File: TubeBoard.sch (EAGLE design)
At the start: 12 parts, among them IC1 HV5530PQFP-44

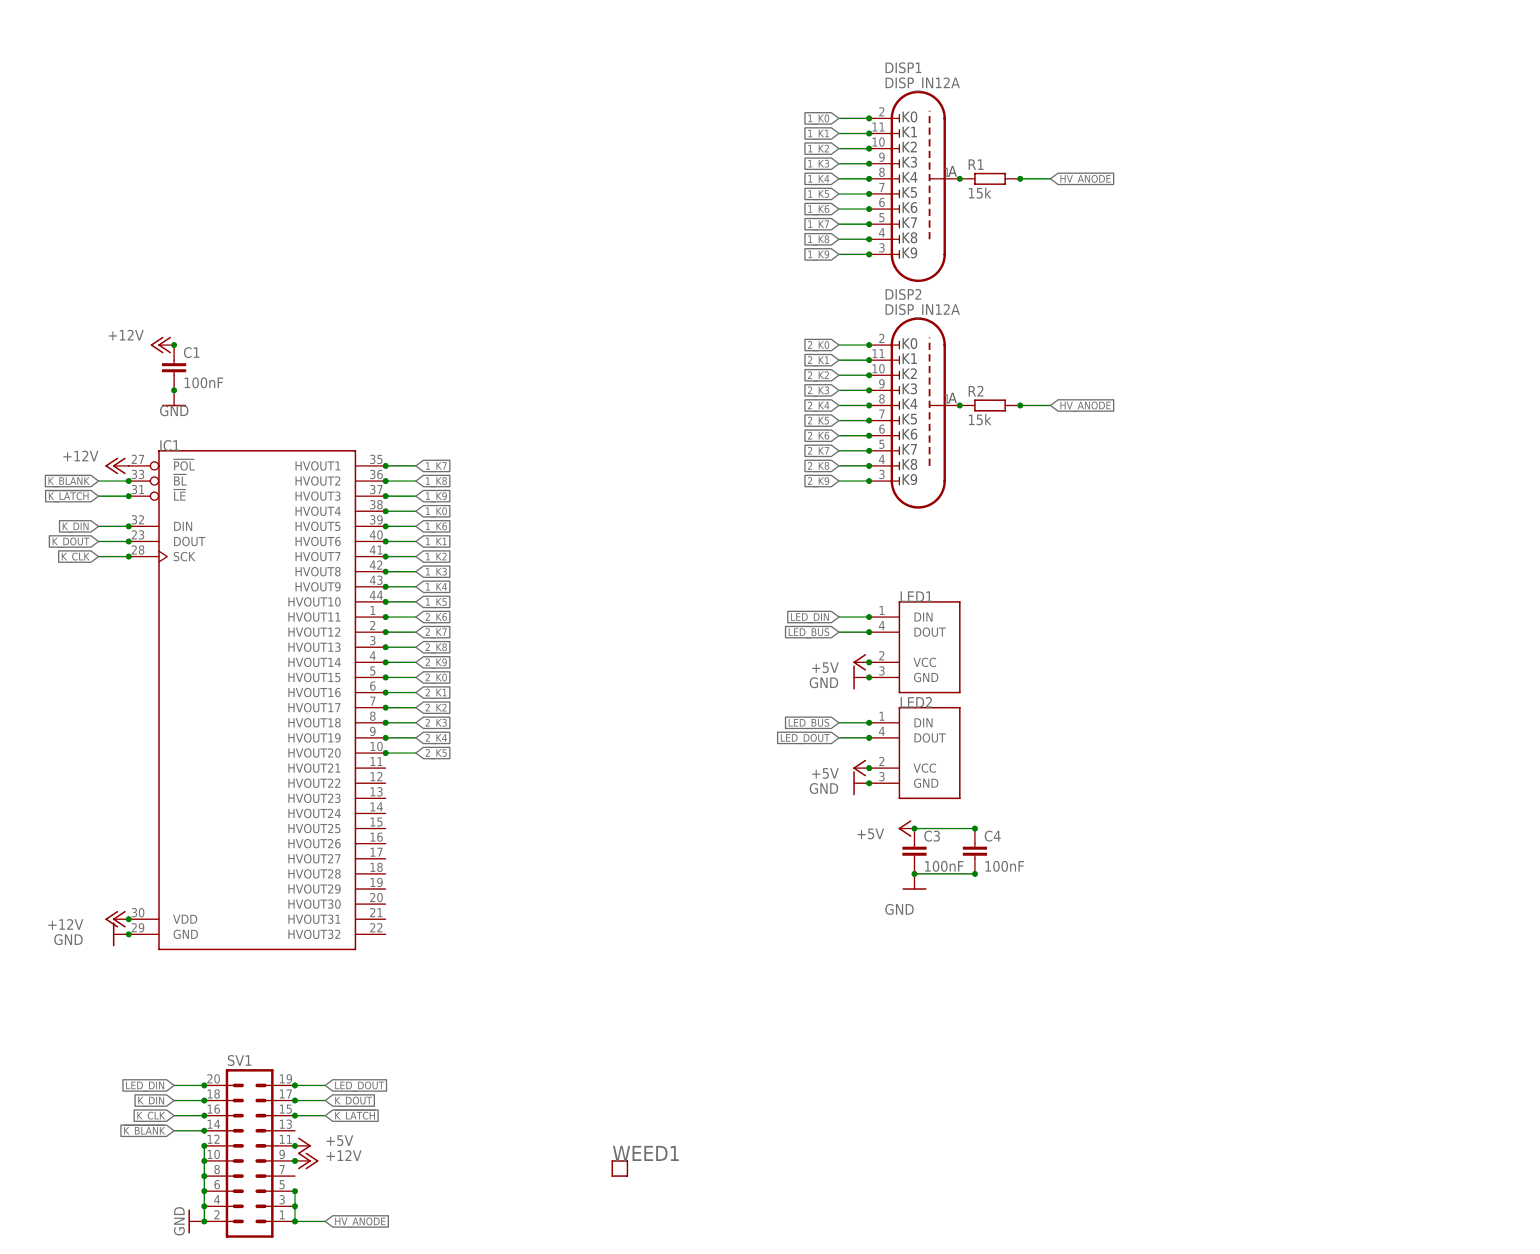
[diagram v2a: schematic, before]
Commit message: Added colons
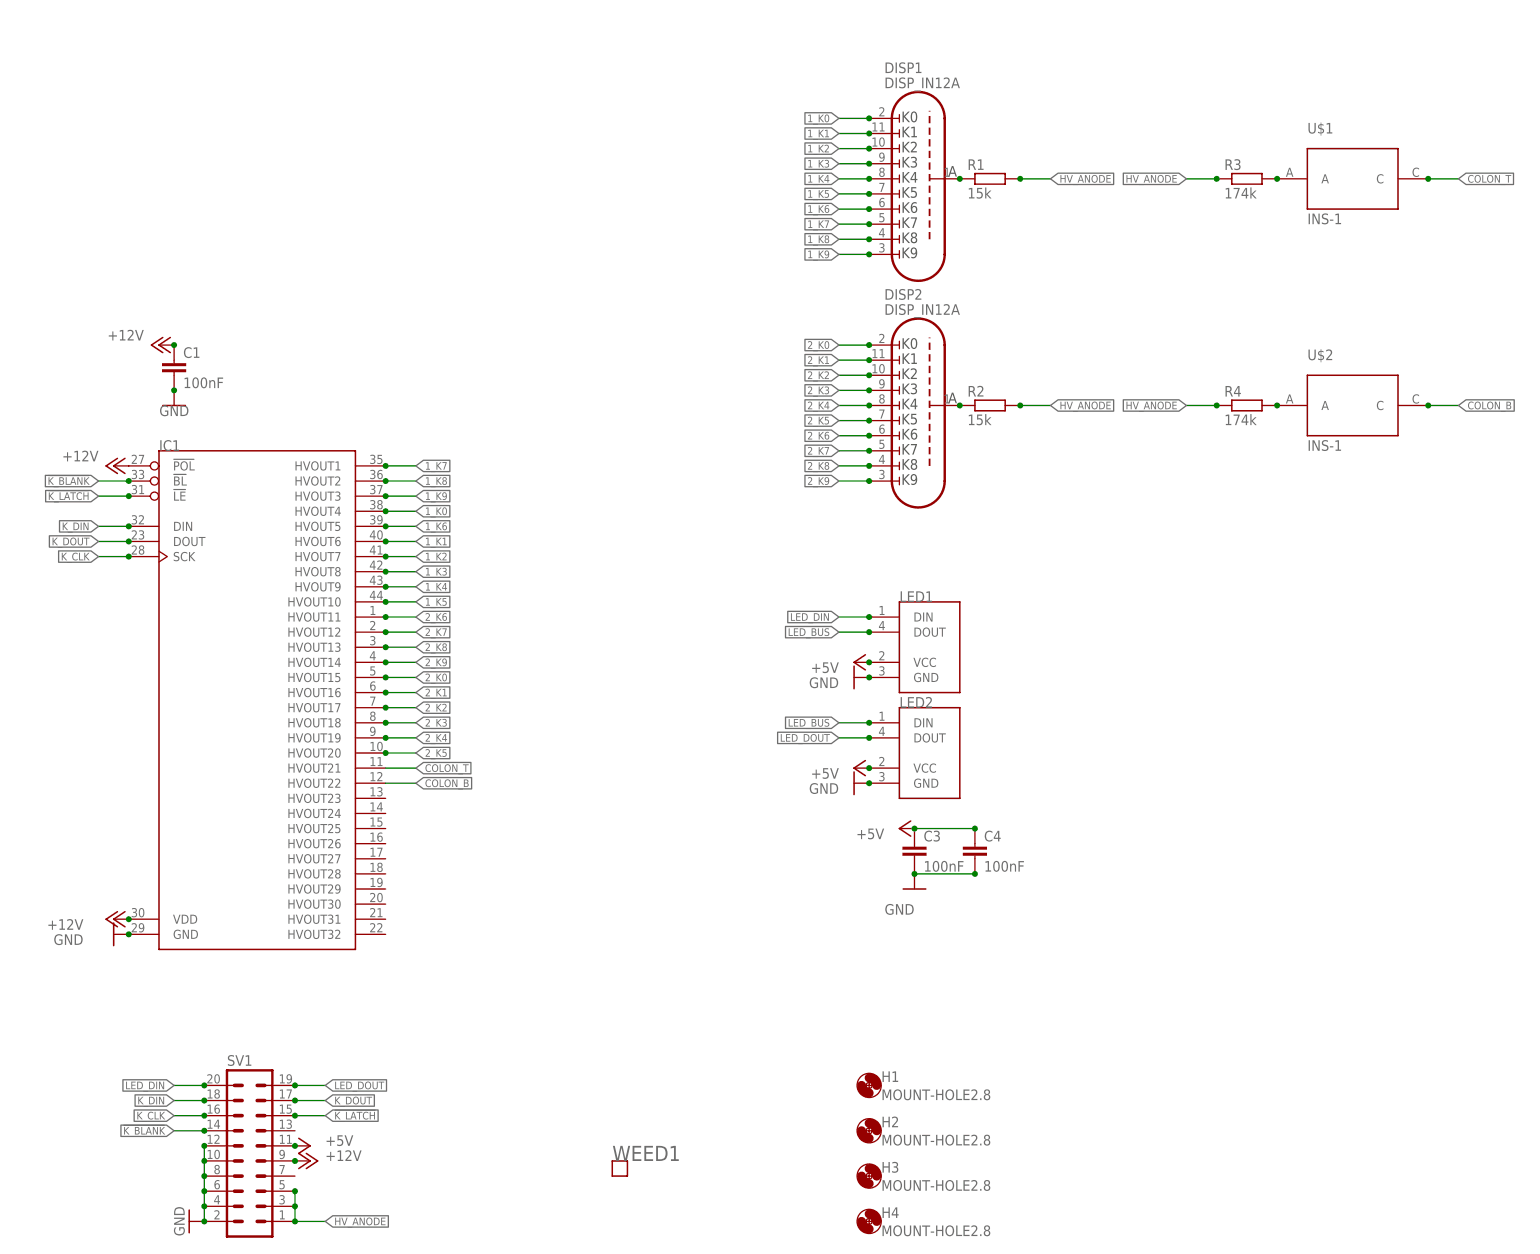
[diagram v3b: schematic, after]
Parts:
- added H1, H2, H3, H4: MOUNT-HOLE2.8, holes:MOUNT-HOLE2.8
- added R3, R4: 174k, rcl:R-EU_M1206
- added U$1, U$2: INS-1, Parts:INS-1
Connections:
- new net COLON_B: IC1.HVOUT22, U$2.C
- new net COLON_T: IC1.HVOUT21, U$1.C
- new net N$3: R3.2, U$1.A
- new net N$4: R4.2, U$2.A
- net HV_ANODE: now also R3.1, R4.1
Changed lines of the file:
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@@
 <part name="P+8" library="supply1" library_urn="urn:adsk.eagle:library:371" deviceset="+5V" device=""/>
 <part name="WEED1" library="Parts" deviceset="WEED" device=""/>
+<part name="U$1" library="Parts" deviceset="INS-1" device=""/>
+<part name="U$2" library="Parts" deviceset="INS-1" device=""/>
+<part name="R3" library="rcl" library_urn="urn:adsk.eagle:library:334" deviceset="R-EU_" device="M1206" package3d_urn="urn:adsk.eagle:package:23566/1" value="174k">
+<spice>
+<pinmapping spiceprefix="R">
+<pinmap gate="G$1" pin="1" pinorder="1"/>
+<pinmap gate="G$1" pin="2" pinorder="2"/>
+</pinmapping>
+</spice>
+<attribute name="MOUSER" value="667-ERJ-8ENF1743V"/>
+</part>
+<part name="R4" library="rcl" library_urn="urn:adsk.eagle:library:334" deviceset="R-EU_" device="M1206" package3d_urn="urn:adsk.eagle:package:23566/1" value="174k">
+<spice>
+<pinmapping spiceprefix="R">
+<pinmap gate="G$1" pin="1" pinorder="1"/>
+<pinmap gate="G$1" pin="2" pinorder="2"/>
+</pinmapping>
+</spice>
+<attribute name="MOUSER" value="667-ERJ-8ENF1743V"/>
+</part>
+<part name="H1" library="holes" library_urn="urn:adsk.eagle:library:237" deviceset="MOUNT-HOLE" device="2.8" package3d_urn="urn:adsk.eagle:package:14271/1"/>
+<part name="H2" library="holes" library_urn="urn:adsk.eagle:library:237" deviceset="MOUNT-HOLE" device="2.8" package3d_urn="urn:adsk.eagle:package:14271/1"/>
+<part name="H3" library="holes" library_urn="urn:adsk.eagle:library:237" deviceset="MOUNT-HOLE" device="2.8" package3d_urn="urn:adsk.eagle:package:14271/1"/>
+<part name="H4" library="holes" library_urn="urn:adsk.eagle:library:237" deviceset="MOUNT-HOLE" device="2.8" package3d_urn="urn:adsk.eagle:package:14271/1"/>
 </parts>
 <sheets>
@@
 </instance>
 <instance part="WEED1" gate="G$1" x="104.14" y="15.24"/>
+<instance part="U$1" gate="G$1" x="228.6" y="182.88"/>
+<instance part="U$2" gate="G$1" x="228.6" y="144.78"/>
+<instance part="R3" gate="G$1" x="210.82" y="182.88">
+<attribute name="MOUSER" x="210.82" y="182.88" size="1.27" layer="96" display="off"/>
+</instance>
+<instance part="R4" gate="G$1" x="210.82" y="144.78">
+<attribute name="MOUSER" x="210.82" y="144.78" size="1.27" layer="96" display="off"/>
+</instance>
+<instance part="H1" gate="G$1" x="147.32" y="30.48"/>
+<instance part="H2" gate="G$1" x="147.32" y="22.86"/>
+<instance part="H3" gate="G$1" x="147.32" y="15.24"/>
+<instance part="H4" gate="G$1" x="147.32" y="7.62"/>
 </instances>
 <busses>
@@
 <label x="177.8" y="182.88" size="1.27" layer="95" xref="yes"/>
 <junction x="172.72" y="182.88"/>
+</segment>
+<segment>
+<wire x1="200.66" y1="182.88" x2="205.74" y2="182.88" width="0.1524" layer="91"/>
+<label x="200.66" y="182.88" size="1.27" layer="95" rot="R180" xref="yes"/>
+<pinref part="R3" gate="G$1" pin="1"/>
+<junction x="205.74" y="182.88"/>
+</segment>
+<segment>
+<wire x1="200.66" y1="144.78" x2="205.74" y2="144.78" width="0.1524" layer="91"/>
+<label x="200.66" y="144.78" size="1.27" layer="95" rot="R180" xref="yes"/>
+<pinref part="R4" gate="G$1" pin="1"/>
+<junction x="205.74" y="144.78"/>
 </segment>
 </net>
@@
 </segment>
 </net>
+<net name="N$3" class="0">
+<segment>
+<pinref part="U$1" gate="G$1" pin="A"/>
+<pinref part="R3" gate="G$1" pin="2"/>
+<junction x="215.9" y="182.88"/>
+</segment>
+</net>
+<net name="N$4" class="0">
+<segment>
+<pinref part="U$2" gate="G$1" pin="A"/>
+<pinref part="R4" gate="G$1" pin="2"/>
+<junction x="215.9" y="144.78"/>
+</segment>
+</net>
+<net name="COLON_T" class="0">
+<segment>
+<pinref part="U$1" gate="G$1" pin="C"/>
+<wire x1="241.3" y1="182.88" x2="246.38" y2="182.88" width="0.1524" layer="91"/>
+<label x="246.38" y="182.88" size="1.27" layer="95" xref="yes"/>
+<junction x="241.3" y="182.88"/>
+</segment>
+<segment>
+<pinref part="IC1" gate="G$1" pin="HVOUT21"/>
+<wire x1="66.04" y1="83.82" x2="71.12" y2="83.82" width="0.1524" layer="91"/>
+<label x="71.12" y="83.82" size="1.27" layer="95" xref="yes"/>
+</segment>
+</net>
+<net name="COLON_B" class="0">
+<segment>
+<pinref part="U$2" gate="G$1" pin="C"/>
+<wire x1="241.3" y1="144.78" x2="246.38" y2="144.78" width="0.1524" layer="91"/>
+<label x="246.38" y="144.78" size="1.27" layer="95" xref="yes"/>
+<junction x="241.3" y="144.78"/>
+</segment>
+<segment>
+<pinref part="IC1" gate="G$1" pin="HVOUT22"/>
+<wire x1="66.04" y1="81.28" x2="71.12" y2="81.28" width="0.1524" layer="91"/>
+<label x="71.12" y="81.28" size="1.27" layer="95" xref="yes"/>
+</segment>
+</net>
